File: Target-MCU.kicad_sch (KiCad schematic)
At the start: 18 parts, among them Q6 DMG1012UW-7, SW5 12V 50mA, U4 CH32V003F4P6

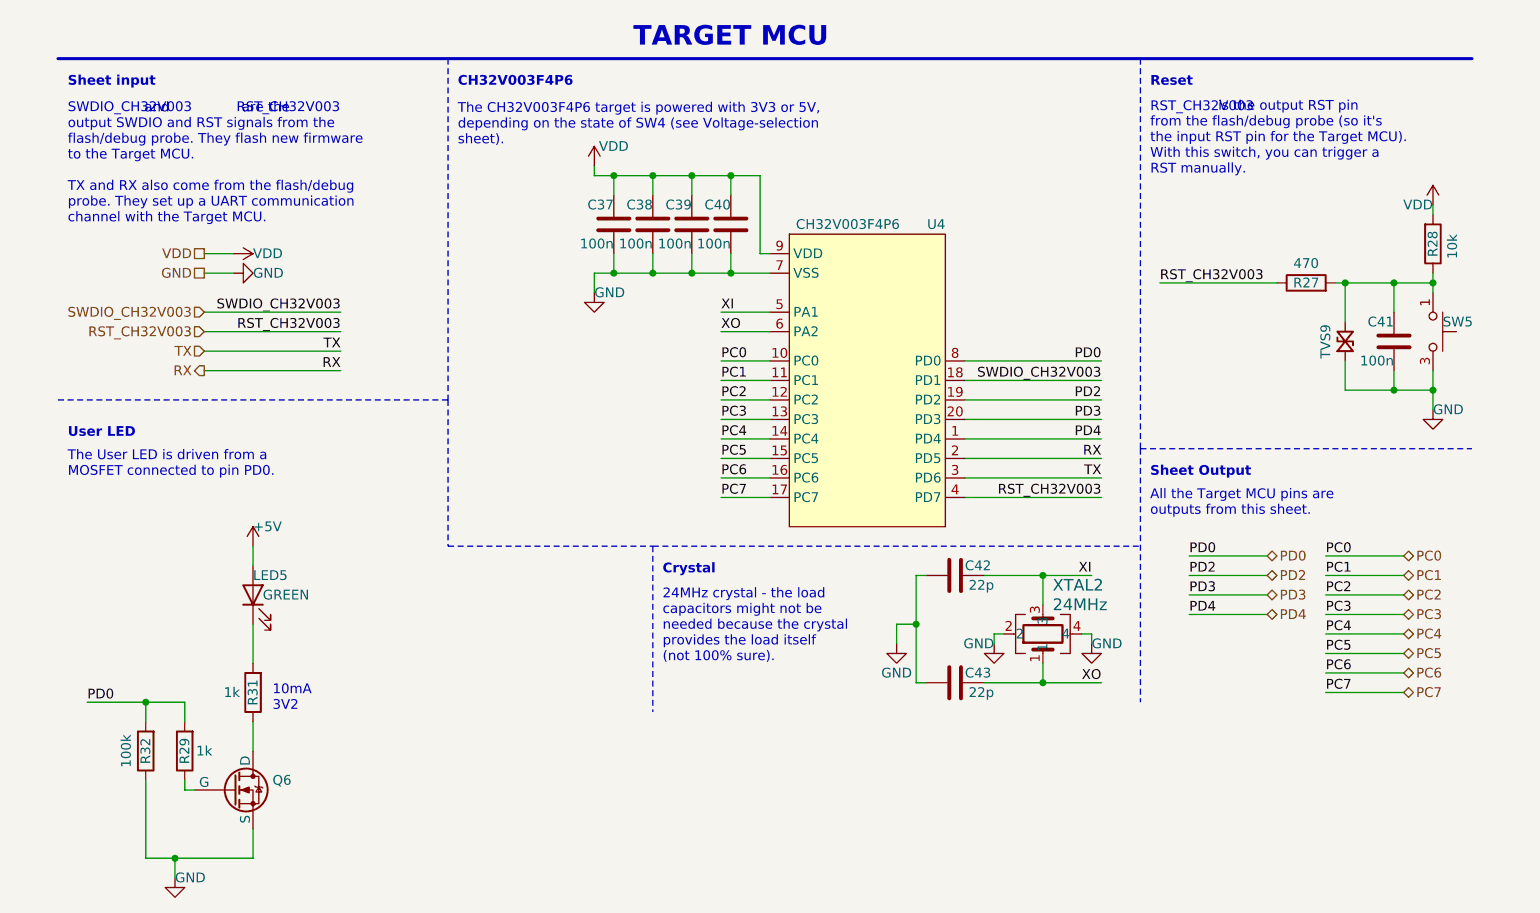
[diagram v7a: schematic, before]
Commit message: Rename 'modify_designators.py' into 'kicad_designators.py'
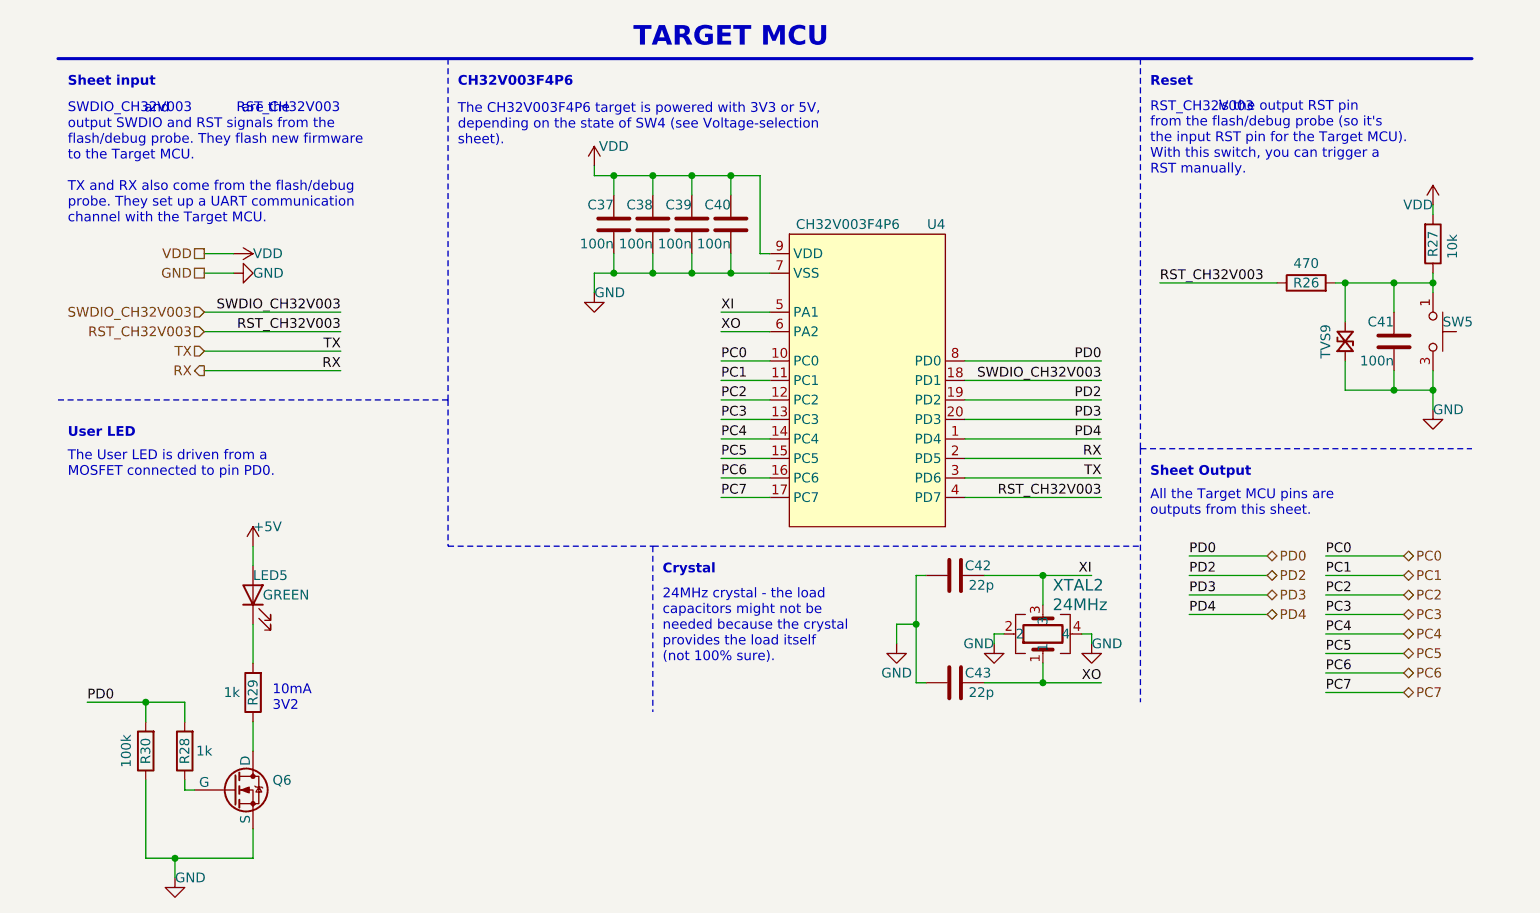
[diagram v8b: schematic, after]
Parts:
- renumbered R27 to R26, R28 to R27, R29 to R28, R31 to R29, R32 to R30
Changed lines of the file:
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@@
   (symbol (lib_id "Device:R") (at 191.77 43.18 0) (mirror x) (unit 1)
     (in_bom yes) (on_board yes) (dnp no)
-    (property "Reference" "R28" (at 191.77 43.18 90)
+    (property "Reference" "R27" (at 191.77 43.18 90)
       (effects (font (size 1.27 1.27)))
     )
@@
       (project "tiny-scarab"
         (path "/156c5422-ee07-49a4-8263-a2dbd26b90bd/d0c4b0c3-1e7e-4a4c-add3-8d4a3a10843d"
+          (reference "R27") (unit 1)
+        )
+      )
+    )
+  )
+  (symbol (lib_id "Device:R") (at 29.21 109.22 180) (unit 1)
+    (in_bom yes) (on_board yes) (dnp no)
+    (property "Reference" "R28" (at 29.21 109.22 90)
+      (effects (font (size 1.27 1.27)))
+    )
+    (property "Value" "1k" (at 31.75 109.22 0)
+      (effects (font (size 1.27 1.27)))
+    )
+    (property "Footprint" "Resistor_SMD:R_0402_1005Metric_Pad0.72x0.64mm_HandSolder" (at 30.988 109.22 90)
+      (effects (font (size 1.27 1.27)) hide)
+    )
+    (property "Datasheet" "~" (at 29.21 109.22 0)
+      (effects (font (size 1.27 1.27)) hide)
+    )
+    (property "MPN" "GPR04021K" (at 29.21 109.22 0)
+      (effects (font (size 1.27 1.27)) hide)
+    )
+    (pin "2")
+    (pin "1")
+    (instances
+      (project "tiny-scarab"
+        (path "/156c5422-ee07-49a4-8263-a2dbd26b90bd/d0c4b0c3-1e7e-4a4c-add3-8d4a3a10843d"
           (reference "R28") (unit 1)
-        )
-      )
-    )
-  )
-  (symbol (lib_id "Device:R") (at 29.21 109.22 180) (unit 1)
-    (in_bom yes) (on_board yes) (dnp no)
-    (property "Reference" "R29" (at 29.21 109.22 90)
-      (effects (font (size 1.27 1.27)))
-    )
-    (property "Value" "1k" (at 31.75 109.22 0)
-      (effects (font (size 1.27 1.27)))
-    )
-    (property "Footprint" "Resistor_SMD:R_0402_1005Metric_Pad0.72x0.64mm_HandSolder" (at 30.988 109.22 90)
-      (effects (font (size 1.27 1.27)) hide)
-    )
-    (property "Datasheet" "~" (at 29.21 109.22 0)
-      (effects (font (size 1.27 1.27)) hide)
-    )
-    (property "MPN" "GPR04021K" (at 29.21 109.22 0)
-      (effects (font (size 1.27 1.27)) hide)
-    )
-    (pin "2")
-    (pin "1")
-    (instances
-      (project "tiny-scarab"
-        (path "/156c5422-ee07-49a4-8263-a2dbd26b90bd/d0c4b0c3-1e7e-4a4c-add3-8d4a3a10843d"
-          (reference "R29") (unit 1)
         )
       )
@@
   (symbol (lib_id "Device:R") (at 175.26 48.26 90) (unit 1)
     (in_bom yes) (on_board yes) (dnp no)
-    (property "Reference" "R27" (at 175.26 48.26 90)
+    (property "Reference" "R26" (at 175.26 48.26 90)
       (effects (font (size 1.27 1.27)))
     )
@@
       (project "tiny-scarab"
         (path "/156c5422-ee07-49a4-8263-a2dbd26b90bd/d0c4b0c3-1e7e-4a4c-add3-8d4a3a10843d"
-          (reference "R27") (unit 1)
+          (reference "R26") (unit 1)
         )
       )
@@
   (symbol (lib_id "Device:R") (at 24.13 109.22 180) (unit 1)
     (in_bom yes) (on_board yes) (dnp no)
-    (property "Reference" "R32" (at 24.13 109.22 90)
+    (property "Reference" "R30" (at 24.13 109.22 90)
       (effects (font (size 1.27 1.27)))
     )
@@
       (project "tiny-scarab"
         (path "/156c5422-ee07-49a4-8263-a2dbd26b90bd/d0c4b0c3-1e7e-4a4c-add3-8d4a3a10843d"
-          (reference "R32") (unit 1)
+          (reference "R30") (unit 1)
         )
       )
@@
   (symbol (lib_id "Device:R") (at 38.1 101.6 180) (unit 1)
     (in_bom yes) (on_board yes) (dnp no)
-    (property "Reference" "R31" (at 38.1 101.6 90)
+    (property "Reference" "R29" (at 38.1 101.6 90)
       (effects (font (size 1.27 1.27)))
     )
@@
       (project "tiny-scarab"
         (path "/156c5422-ee07-49a4-8263-a2dbd26b90bd/d0c4b0c3-1e7e-4a4c-add3-8d4a3a10843d"
-          (reference "R31") (unit 1)
-        )
-      )
+          (reference "R29") (unit 1)
+        )
+      )
